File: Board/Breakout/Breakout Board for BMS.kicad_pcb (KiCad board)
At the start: 2 copper layers, 60.6 x 51.6 mm, 16 parts, among them J1 Conn_01x04, J11 Conn_01x02, J4 Conn_01x03, J7 Conn_01x05, J9 Conn_01x02

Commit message: Breakout updated
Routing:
- net gnd: track 0.00 -> 21.2 mm, vias 18 -> 4
- net (no net): track 187.5 -> 166.2 mm

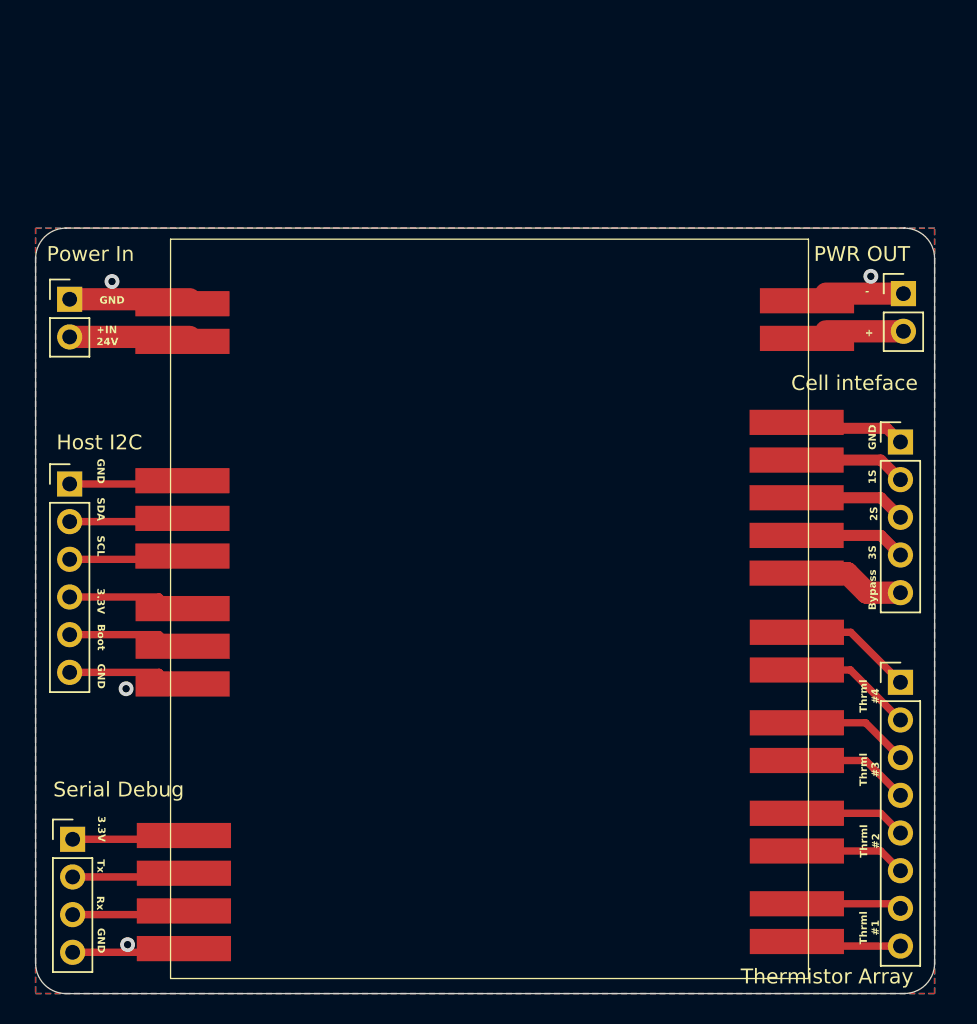
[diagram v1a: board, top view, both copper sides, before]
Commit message: Breakout Rev1 is Ready.
No Errors on DRC, ready to be sent to FAB
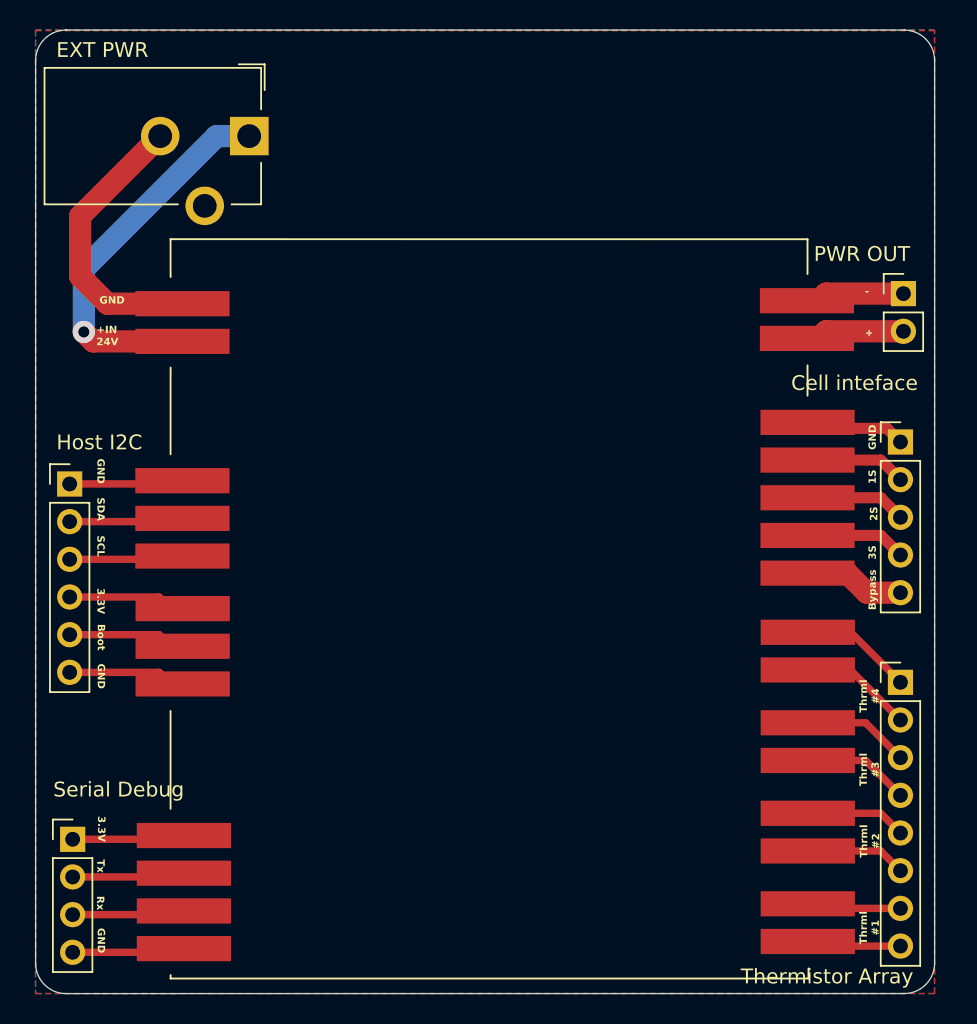
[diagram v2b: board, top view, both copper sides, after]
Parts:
- removed Power In: PinHeader_1x02_P2.54mm_Vertical, Connector_PinHeader_2.54mm:PinHeader_1x02_P2.54mm_Vertical
- added EXT PWR: BarrelJack_CUI_PJ-102AH_Horizontal, Connector_BarrelJack:BarrelJack_CUI_PJ-102AH_Horizontal, F.Cu at (133.9, 26.1)
- moved J11 0.74 mm to (172.3, 77.8)
- moved J7 0.74 mm to (172.3, 45.3)
- moved J9 0.74 mm to (172.3, 71.7)
- moved J9 0.74 mm to (172.3, 59.5)
- moved J9 0.74 mm to (172.3, 65.6)
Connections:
- Cell inteface pad 1: (no net) -> GND
- Cell inteface pad 2: (no net) -> Batt_1s
- Cell inteface pad 3: (no net) -> Batt_2s
- Cell inteface pad 4: (no net) -> Batt_3s
- Cell inteface pad 5: (no net) -> Bypass
- Host I2C pad 1: (no net) -> GND
- Host I2C pad 2: (no net) -> SDA
- Host I2C pad 3: (no net) -> SCL
- Host I2C pad 4: (no net) -> 3.3V_I2C
- Host I2C pad 5: (no net) -> Boot
- Host I2C pad 6: (no net) -> GND
- J1 pad 1: (no net) -> 3.3V
- J1 pad 2: (no net) -> Tx
- J1 pad 3: (no net) -> Rx
- J1 pad 4: (no net) -> GND
- J11 pad 1: (no net) -> Thrml_1
- J11 pad 2: (no net) -> Thrml_2
- J4 pad 1: (no net) -> GND
- J4 pad 2: (no net) -> SDA
- J4 pad 3: (no net) -> SCL
- J4 pad 1: (no net) -> 3.3V_I2C
- J4 pad 2: (no net) -> Boot
- J4 pad 3: (no net) -> GND
- J7 pad 1: (no net) -> GND
- J7 pad 2: (no net) -> Batt_1s
- J7 pad 3: (no net) -> Batt_2s
- J7 pad 4: (no net) -> Batt_3s
- J7 pad 5: (no net) -> Bypass
- J9 pad 1: (no net) -> GND (x2)
- J9 pad 2: (no net) -> 24V
- J9 pad 1: (no net) -> Thrml#2_1
- J9 pad 2: (no net) -> Thrml#2_2
- J9 pad 2: (no net) -> Out
- J9 pad 1: (no net) -> Thrml #4_1
- J9 pad 2: (no net) -> Thrml #4_2
- J9 pad 1: (no net) -> Thrml#3_1
- J9 pad 2: (no net) -> Thrml#3_2
- PWR OUT pad 1: (no net) -> GND
- PWR OUT pad 2: (no net) -> Out
- Serial Debug pad 1: (no net) -> 3.3V
- Serial Debug pad 2: (no net) -> Tx
- Serial Debug pad 3: (no net) -> Rx
- Serial Debug pad 4: (no net) -> GND
- Thermistor Array pad 1: (no net) -> Thrml #4_1
- Thermistor Array pad 2: (no net) -> Thrml #4_2
- Thermistor Array pad 3: (no net) -> Thrml#3_1
- Thermistor Array pad 4: (no net) -> Thrml#3_2
- Thermistor Array pad 5: (no net) -> Thrml#2_1
- Thermistor Array pad 6: (no net) -> Thrml#2_2
- Thermistor Array pad 7: (no net) -> Thrml_1
- Thermistor Array pad 8: (no net) -> Thrml_2
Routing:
- net (no net): track 166.2 -> 0.00 mm
- net GND: track 0.00 -> 54.0 mm
- net 24V: track 0.00 -> 26.8 mm, vias 0 -> 1
- net gnd: track 21.2 -> 0.00 mm, vias 4 -> 0
- net Boot: track 0.00 -> 7.14 mm
- net 3.3V_I2C: track 0.00 -> 7.14 mm
- net SDA: track 0.00 -> 6.89 mm
- net SCL: track 0.00 -> 6.89 mm
- net Thrml #4_1: track 0.00 -> 6.85 mm
- net Thrml #4_2: track 0.00 -> 6.84 mm
- net Tx: track 0.00 -> 6.80 mm
- net Rx: track 0.00 -> 6.80 mm
- net 3.3V: track 0.00 -> 6.80 mm
- net Bypass: track 0.00 -> 6.75 mm
- net Thrml#3_1: track 0.00 -> 6.42 mm
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- added copper zone on F.Cu, net GND
- removed copper zone on F.Cu, net gnd
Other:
- board size 60.6 x 51.6 mm -> 60.6 x 65 mm
